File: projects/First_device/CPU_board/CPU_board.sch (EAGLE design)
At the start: 36 parts, among them IC1 74AC14D, U1 ESP-WROOM-32, X1 2EHDCR-5.08-02P

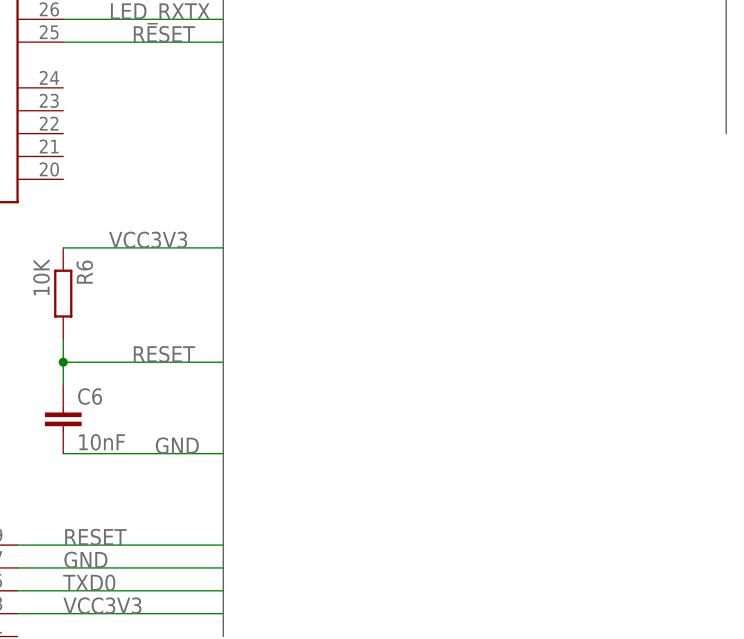
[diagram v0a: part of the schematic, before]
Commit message: Add DO LEDs
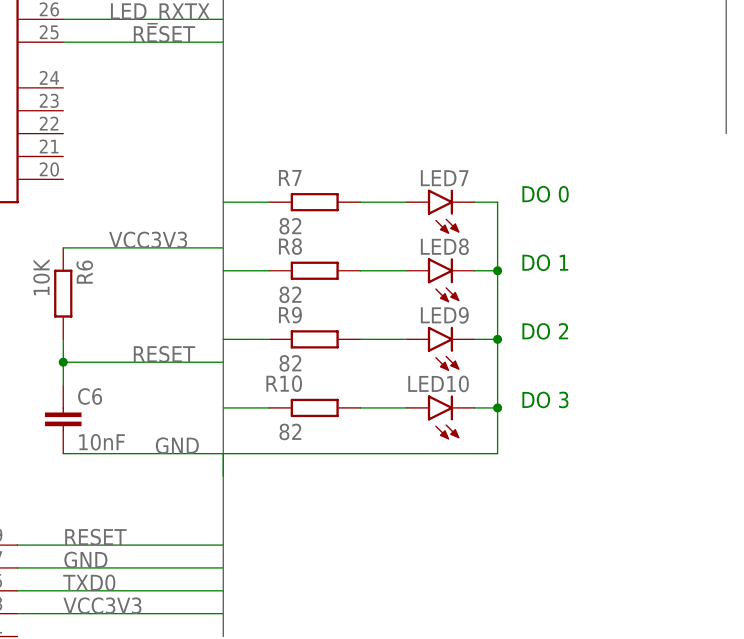
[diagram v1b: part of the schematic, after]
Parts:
- added LED10, LED7, LED8, LED9: (no value), led:LED5MM
- added R10, R7, R8, R9: 82, rcl:R-EU_R0603
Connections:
- new net N$2: LED10.A, R10.1
- new net N$3: LED9.A, R9.1
- new net N$4: LED8.A, R8.1
- new net N$5: LED7.A, R7.1
- net DO0: now also R7.2
- net DO1: now also R8.2
- net DO2: now also R9.2
- net DO3: now also R10.2
- net GND: now also LED10.C, LED7.C, LED8.C, LED9.C
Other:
- note added: "DO 0"
- note added: "DO 1"
- note added: "DO 2"
- note added: "DO 3"
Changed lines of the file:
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@@
 <part name="X1" library="Main-board" deviceset="2EHDCR-5.08-02P" device=""/>
 <part name="JP1" library="pinhead" library_urn="urn:adsk.eagle:library:325" deviceset="PINHD-2X6" device="" package3d_urn="urn:adsk.eagle:package:22474/2"/>
+<part name="R7" library="rcl" library_urn="urn:adsk.eagle:library:334" deviceset="R-EU_" device="R0603" package3d_urn="urn:adsk.eagle:package:23555/3" value="82"/>
+<part name="LED7" library="led" library_urn="urn:adsk.eagle:library:259" deviceset="LED" device="5MM" package3d_urn="urn:adsk.eagle:package:15799/2"/>
+<part name="R8" library="rcl" library_urn="urn:adsk.eagle:library:334" deviceset="R-EU_" device="R0603" package3d_urn="urn:adsk.eagle:package:23555/3" value="82"/>
+<part name="R9" library="rcl" library_urn="urn:adsk.eagle:library:334" deviceset="R-EU_" device="R0603" package3d_urn="urn:adsk.eagle:package:23555/3" value="82"/>
+<part name="R10" library="rcl" library_urn="urn:adsk.eagle:library:334" deviceset="R-EU_" device="R0603" package3d_urn="urn:adsk.eagle:package:23555/3" value="82"/>
+<part name="LED8" library="led" library_urn="urn:adsk.eagle:library:259" deviceset="LED" device="5MM" package3d_urn="urn:adsk.eagle:package:15799/2"/>
+<part name="LED9" library="led" library_urn="urn:adsk.eagle:library:259" deviceset="LED" device="5MM" package3d_urn="urn:adsk.eagle:package:15799/2"/>
+<part name="LED10" library="led" library_urn="urn:adsk.eagle:library:259" deviceset="LED" device="5MM" package3d_urn="urn:adsk.eagle:package:15799/2"/>
 </parts>
 <sheets>
@@
 <text x="5.08" y="-15.24" size="1.778" layer="91">ICSP</text>
 <text x="45.72" y="-50.8" size="1.778" layer="91">RS485</text>
+<text x="71.12" y="17.78" size="1.778" layer="91">DO 0</text>
+<text x="71.12" y="10.16" size="1.778" layer="91">DO 1</text>
+<text x="71.12" y="2.54" size="1.778" layer="91">DO 2</text>
+<text x="71.12" y="-5.08" size="1.778" layer="91">DO 3</text>
 </plain>
 <instances>
@@
 <attribute name="NAME" x="57.15" y="61.595" size="1.778" layer="95"/>
 <attribute name="VALUE" x="57.15" y="40.64" size="1.778" layer="96"/>
+</instance>
+<instance part="R7" gate="G$1" x="48.26" y="17.78" smashed="yes" rot="R180">
+<attribute name="NAME" x="46.99" y="21.3614" size="1.778" layer="95" rot="R180"/>
+<attribute name="VALUE" x="46.99" y="16.002" size="1.778" layer="96" rot="R180"/>
+</instance>
+<instance part="LED7" gate="G$1" x="60.96" y="17.78" smashed="yes" rot="R90">
+<attribute name="NAME" x="65.532" y="21.336" size="1.778" layer="95" rot="R180"/>
+<attribute name="VALUE" x="65.532" y="23.495" size="1.778" layer="96" rot="R180"/>
+</instance>
+<instance part="R8" gate="G$1" x="48.26" y="10.16" smashed="yes" rot="R180">
+<attribute name="NAME" x="46.99" y="13.7414" size="1.778" layer="95" rot="R180"/>
+<attribute name="VALUE" x="46.99" y="8.382" size="1.778" layer="96" rot="R180"/>
+</instance>
+<instance part="R9" gate="G$1" x="48.26" y="2.54" smashed="yes" rot="R180">
+<attribute name="NAME" x="46.99" y="6.1214" size="1.778" layer="95" rot="R180"/>
+<attribute name="VALUE" x="46.99" y="0.762" size="1.778" layer="96" rot="R180"/>
+</instance>
+<instance part="R10" gate="G$1" x="48.26" y="-5.08" smashed="yes" rot="R180">
+<attribute name="NAME" x="46.99" y="-1.4986" size="1.778" layer="95" rot="R180"/>
+<attribute name="VALUE" x="46.99" y="-6.858" size="1.778" layer="96" rot="R180"/>
+</instance>
+<instance part="LED8" gate="G$1" x="60.96" y="10.16" smashed="yes" rot="R90">
+<attribute name="NAME" x="65.532" y="13.716" size="1.778" layer="95" rot="R180"/>
+<attribute name="VALUE" x="65.532" y="15.875" size="1.778" layer="96" rot="R180"/>
+</instance>
+<instance part="LED9" gate="G$1" x="60.96" y="2.54" smashed="yes" rot="R90">
+<attribute name="NAME" x="65.532" y="6.096" size="1.778" layer="95" rot="R180"/>
+<attribute name="VALUE" x="65.532" y="8.255" size="1.778" layer="96" rot="R180"/>
+</instance>
+<instance part="LED10" gate="G$1" x="60.96" y="-5.08" smashed="yes" rot="R90">
+<attribute name="NAME" x="65.532" y="-1.524" size="1.778" layer="95" rot="R180"/>
+<attribute name="VALUE" x="65.532" y="0.635" size="1.778" layer="96" rot="R180"/>
 </instance>
 </instances>
@@
 <wire x1="68.58" y1="48.26" x2="93.98" y2="48.26" width="0.1524" layer="91"/>
 <label x="76.2" y="48.26" size="1.778" layer="95"/>
+</segment>
+<segment>
+<wire x1="38.1" y1="-12.7" x2="38.1" y2="-10.16" width="0.1524" layer="91"/>
+<wire x1="38.1" y1="-10.16" x2="68.58" y2="-10.16" width="0.1524" layer="91"/>
+<pinref part="LED7" gate="G$1" pin="C"/>
+<wire x1="66.04" y1="17.78" x2="68.58" y2="17.78" width="0.1524" layer="91"/>
+<pinref part="LED8" gate="G$1" pin="C"/>
+<wire x1="68.58" y1="17.78" x2="68.58" y2="10.16" width="0.1524" layer="91"/>
+<wire x1="68.58" y1="10.16" x2="66.04" y2="10.16" width="0.1524" layer="91"/>
+<pinref part="LED9" gate="G$1" pin="C"/>
+<wire x1="68.58" y1="10.16" x2="68.58" y2="2.54" width="0.1524" layer="91"/>
+<wire x1="68.58" y1="2.54" x2="66.04" y2="2.54" width="0.1524" layer="91"/>
+<junction x="68.58" y="10.16"/>
+<pinref part="LED10" gate="G$1" pin="C"/>
+<wire x1="68.58" y1="2.54" x2="68.58" y2="-5.08" width="0.1524" layer="91"/>
+<wire x1="68.58" y1="-5.08" x2="66.04" y2="-5.08" width="0.1524" layer="91"/>
+<junction x="68.58" y="2.54"/>
+<wire x1="68.58" y1="-10.16" x2="68.58" y2="-5.08" width="0.1524" layer="91"/>
+<junction x="68.58" y="-5.08"/>
 </segment>
 </net>
@@
 <label x="76.2" y="58.42" size="1.778" layer="95"/>
 </segment>
+<segment>
+<pinref part="R7" gate="G$1" pin="2"/>
+<wire x1="43.18" y1="17.78" x2="38.1" y2="17.78" width="0.1524" layer="91"/>
+</segment>
 </net>
 <net name="DO1" class="0">
@@
 <label x="76.2" y="55.88" size="1.778" layer="95"/>
 </segment>
+<segment>
+<pinref part="R8" gate="G$1" pin="2"/>
+<wire x1="43.18" y1="10.16" x2="38.1" y2="10.16" width="0.1524" layer="91"/>
+</segment>
 </net>
 <net name="DO2" class="0">
@@
 <label x="76.2" y="53.34" size="1.778" layer="95"/>
 </segment>
+<segment>
+<pinref part="R9" gate="G$1" pin="2"/>
+<wire x1="43.18" y1="2.54" x2="38.1" y2="2.54" width="0.1524" layer="91"/>
+</segment>
 </net>
 <net name="DO3" class="0">
@@
 <wire x1="68.58" y1="50.8" x2="93.98" y2="50.8" width="0.1524" layer="91"/>
 <label x="76.2" y="50.8" size="1.778" layer="95"/>
+</segment>
+<segment>
+<pinref part="R10" gate="G$1" pin="2"/>
+<wire x1="43.18" y1="-5.08" x2="38.1" y2="-5.08" width="0.1524" layer="91"/>
 </segment>
 </net>
@@
 </segment>
 </net>
+<net name="N$2" class="0">
+<segment>
+<pinref part="R10" gate="G$1" pin="1"/>
+<pinref part="LED10" gate="G$1" pin="A"/>
+<wire x1="53.34" y1="-5.08" x2="58.42" y2="-5.08" width="0.1524" layer="91"/>
+</segment>
+</net>
+<net name="N$3" class="0">
+<segment>
+<pinref part="R9" gate="G$1" pin="1"/>
+<pinref part="LED9" gate="G$1" pin="A"/>
+<wire x1="53.34" y1="2.54" x2="58.42" y2="2.54" width="0.1524" layer="91"/>
+</segment>
+</net>
+<net name="N$4" class="0">
+<segment>
+<pinref part="R8" gate="G$1" pin="1"/>
+<pinref part="LED8" gate="G$1" pin="A"/>
+<wire x1="53.34" y1="10.16" x2="58.42" y2="10.16" width="0.1524" layer="91"/>
+</segment>
+</net>
+<net name="N$5" class="0">
+<segment>
+<pinref part="R7" gate="G$1" pin="1"/>
+<pinref part="LED7" gate="G$1" pin="A"/>
+<wire x1="53.34" y1="17.78" x2="58.42" y2="17.78" width="0.1524" layer="91"/>
+</segment>
+</net>

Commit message: More changes
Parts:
- removed C10: 0,1uF, rcl:C-EUC0603
- removed R33, R55, R77: 82, rcl:R-EU_R0603
- removed U$1: LD1117V33, LD1117V33:LD1117V33
- added R12, R13: 10K, rcl:R-EU_R0603
- added R14, R15, R16, R17: 330, rcl:R-EU_R0603
- added U2: LD1117V33C, LD1117V33:LD1117V33C
- C1: value 10nF -> 0,1uF
- C2: value 0.1uF -> 22uF 10V; device rcl:C-EUC0603 -> rcl:CPOL-EUA
- C4, C7: value 22uF 10V -> 0,1uF; device rcl:CPOL-EUD -> rcl:C-EUC0603
- C6: value 10nF -> 1uF
- C8: value 0,1uF -> 22uF 10V; device rcl:C-EUC0603 -> rcl:CPOL-EUD
- C9: value 1uF -> 0,1uF
- R1, R2, R3, R4, R7, R8: value 82 -> 330
- R10, R11, R9: value 82 -> 10K
- R5, R6: value 10K -> 330
- U4: value AM1/4L -> AM1/4L-0505S-NZ
- renumbered U$2 to U3, U$3 to U4
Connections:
- new net REDE: R10.1, U1.IO21, U3.DE, U3.RE
- net DIN0: now also U1.IO23; no longer U1.SENSOR_VN
- net DO0: now also R14.2; no longer R7.2
- net DO1: now also R15.2; no longer R8.2
- net DO2: now also R16.2; no longer R9.2
- net DO3: now also R17.2; no longer R10.2
- net EN: now also C4.1, R9.2; no longer C1.1, R5.2
- net GND: now also C2.-, C4.2, R10.2, U2.GND; no longer C2.2, C4.-, C6.2, U$1.GND, U3.DE, U3.RE
- net LED_RXTX: now also R6.1; no longer R2.1
- net LED_STGREEN: now also R7.1; no longer R3.1
- net LED_STRED: now also R8.1; no longer R4.1
- net N$1: now also R1.1; no longer R11.1
- net N$10: now also R7.2; no longer R3.2
- net N$11: now also R8.2; no longer R4.2
- net N$12: now also R5.2; no longer R1.2
- net N$13: now also C8.+, C9.1, R13.2; no longer C7.+, C8.1
- net N$14: now also C6.2, C7.2, C8.-, R12.2; no longer C10.2, C7.-, C8.2
- net N$15: now also C6.1, C7.1; no longer C10.1, C9.1
- net N$16: now also R13.1, U3.Y
- net N$17: now also R12.1, U3.Z
- net N$2: now also R17.1; no longer R10.1
- net N$3: now also R16.1; no longer R9.1
- net N$4: now also R15.1; no longer R8.1
- net N$5: now also R14.1; no longer R7.1
- net N$6: now also R2.1; no longer R33.1
- net N$7: now also R3.1; no longer R55.1
- net N$8: now also R4.1; no longer R77.1
- net N$9: now also R6.2; no longer R2.2
- net RESET: now also C5.1, R11.2; no longer C2.1, C6.1, R6.2
- net SBA: now also U1.IO22; no longer U1.SENSOR_VP
- net VCC3V3: now also C2.+, R1.2, R11.1, R2.2, R3.2, R4.2, R9.1, U2.OUT; no longer C4.+, R1.1, R11.2, R33.2, R55.2, R6.1, R77.2, U$1.OUT
- net VCC5: now also C1.1, U2.IN; no longer C5.1, U$1.IN
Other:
- moved on the sheet: C1, C5, C6, C9, R1, R10, R11, R2, R3, R4, R5, R6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

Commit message: Add ATEC608
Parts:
- added R18, R19: 2.4k, rcl:R-EU_R0603
- added U5: ATECC608A, atecc:ATECC608A
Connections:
- new net SCL: R18.1, U1.IO22, U5.SCL
- new net SDA: R19.1, U1.IO21, U5.SDA
- net GND: now also U5.GND
- net REDE: now also U1.IO2; no longer U1.IO21
- net SBA: now also U1.IO15; no longer U1.IO22
- net VCC3V3: now also R18.2, R19.2, U5.VCC
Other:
- note added: "*"
- moved on the sheet: LED10, LED7, LED8, LED9, R14, R15, R16, R17
